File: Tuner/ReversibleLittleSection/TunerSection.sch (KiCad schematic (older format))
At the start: 119 parts, among them J1 Conn_01x03, J10 Conn_01x02, J11 Conn_02x05_Odd_Even, J12 Conn_01x01, J13 Conn_01x01, J14 Conn_01x01, J15 Conn_01x01, J16 Conn_01x01, J17 Conn_01x01, J18 Conn_01x01, J19 Conn_01x01, J2 Conn_01x03, J20 Conn_01x01, J21 Conn_01x01, J22 Conn_01x01, J23 Conn_01x02, J3 Conn_01x03, J4 Conn_01x03, J5 Conn_01x03, J6 Conn_01x03, J7 Conn_01x03, J8 Conn_01x02, J9 Conn_01x02, P10 Conn_01x01, P11 Conn_01x01, P12 Conn_01x01, P2 Conn_01x01, P3 Conn_01x01, P4 Conn_01x01, P5 Conn_01x01, P6 Conn_01x01, P7 Conn_01x01, P8 Conn_01x01, P9 Conn_01x01, U1 MCP23008, U2 ULN2803A

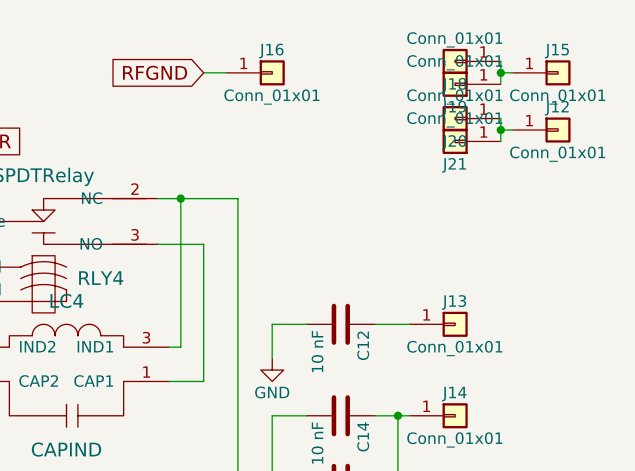
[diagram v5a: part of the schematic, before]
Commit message: Added extra capacitors between relay power and ground posts
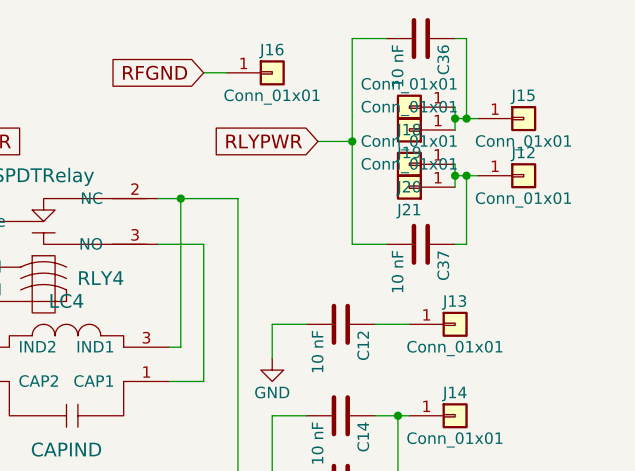
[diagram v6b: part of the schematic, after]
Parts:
- added C36, C37: 10 nF, Capacitors_THT:C_Disc_D5.0mm_W2.5mm_P2.50mm, symbol C
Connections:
- net RLYPWR: now also C36.2, C37.2
- net at J15.1 (Pin_1), J18.1 (Pin_1), J19.1 (Pin_1): now also C36.1
- net at J12.1 (Pin_1), J20.1 (Pin_1), J21.1 (Pin_1): now also C37.1
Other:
- moved on the sheet: J12, J15, J18, J19, J20, J21
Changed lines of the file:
@@
 $EndComp
 $Comp
-L +5V #PWR17
+L +5V #PWR16
 U 1 1 5B1ABFC6
 P 8800 4600
-F 0 "#PWR17" H 8800 4450 50  0001 C CNN
+F 0 "#PWR16" H 8800 4450 50  0001 C CNN
 F 1 "+5V" H 8800 4740 50  0000 C CNN
 F 2 "" H 8800 4600 50  0001 C CNN
@@
 $EndComp
 $Comp
-L GND #PWR18
+L GND #PWR17
 U 1 1 5B1AC04C
 P 8800 5050
-F 0 "#PWR18" H 8800 4800 50  0001 C CNN
+F 0 "#PWR17" H 8800 4800 50  0001 C CNN
 F 1 "GND" H 8800 4900 50  0000 C CNN
 F 2 "" H 8800 5050 50  0001 C CNN
@@
 L Conn_01x01 J15
 U 1 1 5B19812D
-P 11100 750
-F 0 "J15" H 11100 850 50  0000 C CNN
-F 1 "Conn_01x01" H 11100 650 50  0000 C CNN
-F 2 "Connectors:1pin" H 11100 750 50  0001 C CNN
-F 3 "" H 11100 750 50  0001 C CNN
-	1    11100 750
+P 10950 950
+F 0 "J15" H 10950 1050 50  0000 C CNN
+F 1 "Conn_01x01" H 10950 850 50  0000 C CNN
+F 2 "Connectors:1pin" H 10950 950 50  0001 C CNN
+F 3 "" H 10950 950 50  0001 C CNN
+	1    10950 950
 	1    0    0    -1
 $EndComp
@@
 $EndComp
 $Comp
-L GND #PWR19
+L GND #PWR18
 U 1 1 5B982525
 P 9850 2000
-F 0 "#PWR19" H 9850 1750 50  0001 C CNN
+F 0 "#PWR18" H 9850 1750 50  0001 C CNN
 F 1 "GND" H 9850 1850 50  0000 C CNN
 F 2 "" H 9850 2000 50  0001 C CNN
@@
 L Conn_01x01 J18
 U 1 1 5BD8893E
-P 10650 700
-F 0 "J18" H 10650 800 50  0000 C CNN
-F 1 "Conn_01x01" H 10650 600 50  0000 C CNN
-F 2 "tuner:SOLDERJUMPER" H 10650 700 50  0001 C CNN
-F 3 "" H 10650 700 50  0001 C CNN
-	1    10650 700
+P 10450 900
+F 0 "J18" H 10450 1000 50  0000 C CNN
+F 1 "Conn_01x01" H 10450 800 50  0000 C CNN
+F 2 "tuner:SOLDERJUMPER" H 10450 900 50  0001 C CNN
+F 3 "" H 10450 900 50  0001 C CNN
+	1    10450 900
 	-1   0    0    1
 $EndComp
@@
 L Conn_01x01 J19
 U 1 1 5BD88AB6
-P 10650 800
-F 0 "J19" H 10650 900 50  0000 C CNN
-F 1 "Conn_01x01" H 10650 700 50  0000 C CNN
-F 2 "tuner:SOLDERJUMPER" H 10650 800 50  0001 C CNN
-F 3 "" H 10650 800 50  0001 C CNN
-	1    10650 800
+P 10450 1000
+F 0 "J19" H 10450 1100 50  0000 C CNN
+F 1 "Conn_01x01" H 10450 900 50  0000 C CNN
+F 2 "tuner:SOLDERJUMPER" H 10450 1000 50  0001 C CNN
+F 3 "" H 10450 1000 50  0001 C CNN
+	1    10450 1000
 	-1   0    0    1
 $EndComp
@@
 L Conn_01x01 J20
 U 1 1 5BD8922D
-P 10650 950
-F 0 "J20" H 10650 1050 50  0000 C CNN
-F 1 "Conn_01x01" H 10650 850 50  0000 C CNN
-F 2 "tuner:SOLDERJUMPER" H 10650 950 50  0001 C CNN
-F 3 "" H 10650 950 50  0001 C CNN
-	1    10650 950
+P 10450 1150
+F 0 "J20" H 10450 1250 50  0000 C CNN
+F 1 "Conn_01x01" H 10450 1050 50  0000 C CNN
+F 2 "tuner:SOLDERJUMPER" H 10450 1150 50  0001 C CNN
+F 3 "" H 10450 1150 50  0001 C CNN
+	1    10450 1150
 	-1   0    0    1
 $EndComp
@@
 L Conn_01x01 J21
 U 1 1 5BD8939E
-P 10650 1050
-F 0 "J21" H 10650 1150 50  0000 C CNN
-F 1 "Conn_01x01" H 10650 950 50  0000 C CNN
-F 2 "tuner:SOLDERJUMPER" H 10650 1050 50  0001 C CNN
-F 3 "" H 10650 1050 50  0001 C CNN
-	1    10650 1050
+P 10450 1250
+F 0 "J21" H 10450 1350 50  0000 C CNN
+F 1 "Conn_01x01" H 10450 1150 50  0000 C CNN
+F 2 "tuner:SOLDERJUMPER" H 10450 1250 50  0001 C CNN
+F 3 "" H 10450 1250 50  0001 C CNN
+	1    10450 1250
 	-1   0    0    1
 $EndComp
@@
 L Conn_01x01 J12
 U 1 1 5BD8A2D9
-P 11100 1000
-F 0 "J12" H 11100 1100 50  0000 C CNN
-F 1 "Conn_01x01" H 11100 900 50  0000 C CNN
-F 2 "Connectors:1pin" H 11100 1000 50  0001 C CNN
-F 3 "" H 11100 1000 50  0001 C CNN
-	1    11100 1000
-	1    0    0    -1
+P 10950 1200
+F 0 "J12" H 10950 1300 50  0000 C CNN
+F 1 "Conn_01x01" H 10950 1100 50  0000 C CNN
+F 2 "Connectors:1pin" H 10950 1200 50  0001 C CNN
+F 3 "" H 10950 1200 50  0001 C CNN
+	1    10950 1200
+	1    0    0    -1
+$EndComp
+$Comp
+L Conn_01x02 J23
+U 1 1 5C9BB02B
+P 8400 2700
+F 0 "J23" H 8400 2800 50  0000 C CNN
+F 1 "Conn_01x02" H 8400 2500 50  0000 C CNN
+F 2 "tuner:bnc_90_1-1337543-0_pad_combo" H 8400 2700 50  0001 C CNN
+F 3 "" H 8400 2700 50  0001 C CNN
+	1    8400 2700
+	-1   0    0    -1
+$EndComp
+Text GLabel 8950 2800 2    60   Input ~ 0
+RFGND
+Text GLabel 10050 1050 0    60   Input ~ 0
+RLYPWR
+$Comp
+L C C36
+U 1 1 5DDBF507
+P 10500 600
+F 0 "C36" H 10525 700 50  0000 L CNN
+F 1 "10 nF" H 10525 500 50  0000 L CNN
+F 2 "Capacitors_THT:C_Disc_D5.0mm_W2.5mm_P2.50mm" H 10538 450 50  0001 C CNN
+F 3 "" H 10500 600 50  0001 C CNN
+	1    10500 600
+	0    1    1    0
+$EndComp
+$Comp
+L C C37
+U 1 1 5DDBF789
+P 10500 1500
+F 0 "C37" H 10525 1600 50  0000 L CNN
+F 1 "10 nF" H 10525 1400 50  0000 L CNN
+F 2 "Capacitors_THT:C_Disc_D5.0mm_W2.5mm_P2.50mm" H 10538 1350 50  0001 C CNN
+F 3 "" H 10500 1500 50  0001 C CNN
+	1    10500 1500
+	0    1    1    0
 $EndComp
 Connection ~ 10200 5350
@@
 	9650 750  9550 750
 Wire Wire Line
-	10850 700  10850 800
-Wire Wire Line
-	10850 750  10900 750
-Connection ~ 10850 750
-Wire Wire Line
-	10850 950  10850 1050
-Wire Wire Line
-	10850 1000 10900 1000
-Connection ~ 10850 1000
+	10650 900  10650 1000
+Wire Wire Line
+	10650 950  10750 950
+Connection ~ 10650 950
+Wire Wire Line
+	10650 1150 10650 1250
+Wire Wire Line
+	10650 1200 10750 1200
+Connection ~ 10650 1200
 Wire Wire Line
 	10300 4000 10150 4000
@@
 	1850 5200 1850 5300
 Connection ~ 850  5500
-$Comp
-L Conn_01x02 J23
-U 1 1 5C9BB02B
-P 8400 2700
-F 0 "J23" H 8400 2800 50  0000 C CNN
-F 1 "Conn_01x02" H 8400 2500 50  0000 C CNN
-F 2 "tuner:bnc_90_1-1337543-0_pad_combo" H 8400 2700 50  0001 C CNN
-F 3 "" H 8400 2700 50  0001 C CNN
-	1    8400 2700
-	-1   0    0    -1
-$EndComp
 Wire Wire Line
 	8600 2700 8700 2700
@@
 	8500 3100 8500 3200
 Connection ~ 8500 3200
-Text GLabel 8950 2800 2    60   Input ~ 0
-RFGND
 Wire Wire Line
 	8950 2800 8600 2800
+Wire Wire Line
+	10200 1500 10350 1500
+Wire Wire Line
+	10200 600  10200 1500
+Wire Wire Line
+	10200 600  10350 600
+Wire Wire Line
+	10200 1050 10050 1050
+Connection ~ 10200 1050
+Wire Wire Line
+	10700 950  10700 600
+Wire Wire Line
+	10700 600  10650 600
+Connection ~ 10700 950
+Wire Wire Line
+	10700 1200 10700 1500
+Wire Wire Line
+	10700 1500 10650 1500
+Connection ~ 10700 1200
 $EndSCHEMATC

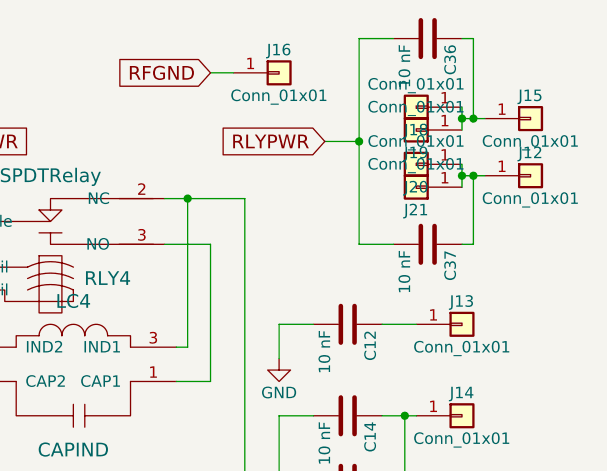
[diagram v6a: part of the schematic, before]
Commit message: Changed some of the capacitors to NC becaue they might cause problems in some situations
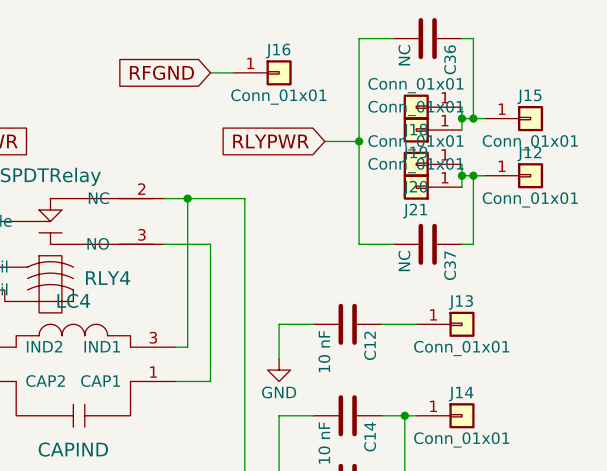
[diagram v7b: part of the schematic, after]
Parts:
- C36, C37: value 10 nF -> NC
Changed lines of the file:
@@
 P 10500 600
 F 0 "C36" H 10525 700 50  0000 L CNN
-F 1 "10 nF" H 10525 500 50  0000 L CNN
+F 1 "NC" H 10525 500 50  0000 L CNN
 F 2 "Capacitors_THT:C_Disc_D5.0mm_W2.5mm_P2.50mm" H 10538 450 50  0001 C CNN
 F 3 "" H 10500 600 50  0001 C CNN
@@
 P 10500 1500
 F 0 "C37" H 10525 1600 50  0000 L CNN
-F 1 "10 nF" H 10525 1400 50  0000 L CNN
+F 1 "NC" H 10525 1400 50  0000 L CNN
 F 2 "Capacitors_THT:C_Disc_D5.0mm_W2.5mm_P2.50mm" H 10538 1350 50  0001 C CNN
 F 3 "" H 10500 1500 50  0001 C CNN

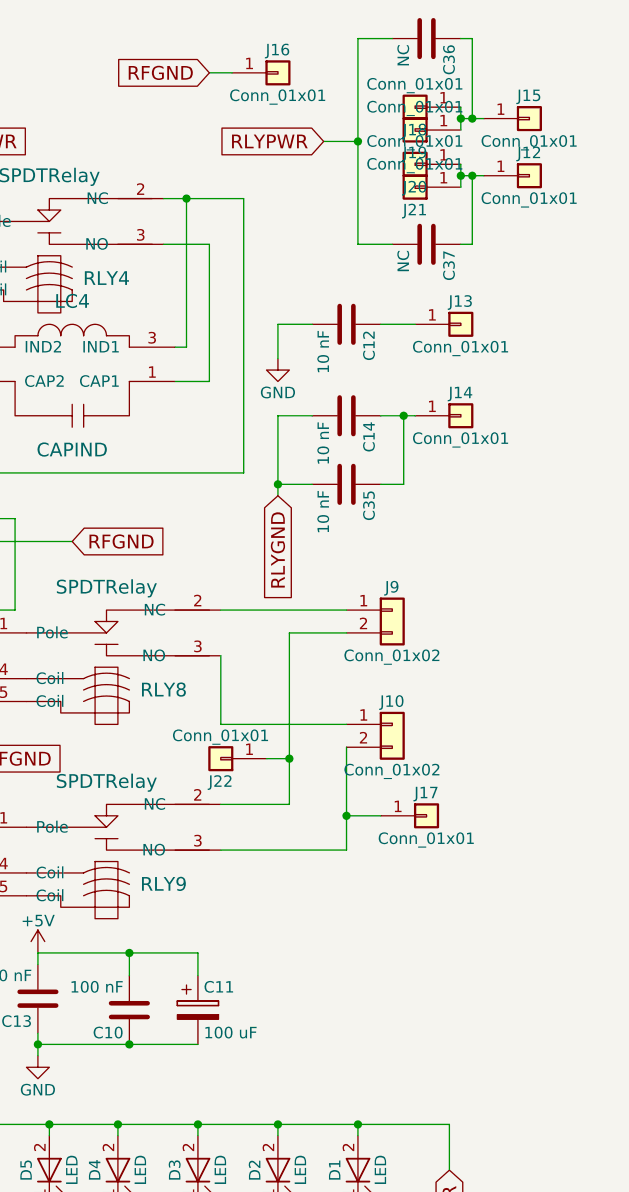
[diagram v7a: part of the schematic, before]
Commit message: Added extra mounting holes to ground ReversibleLittleSection
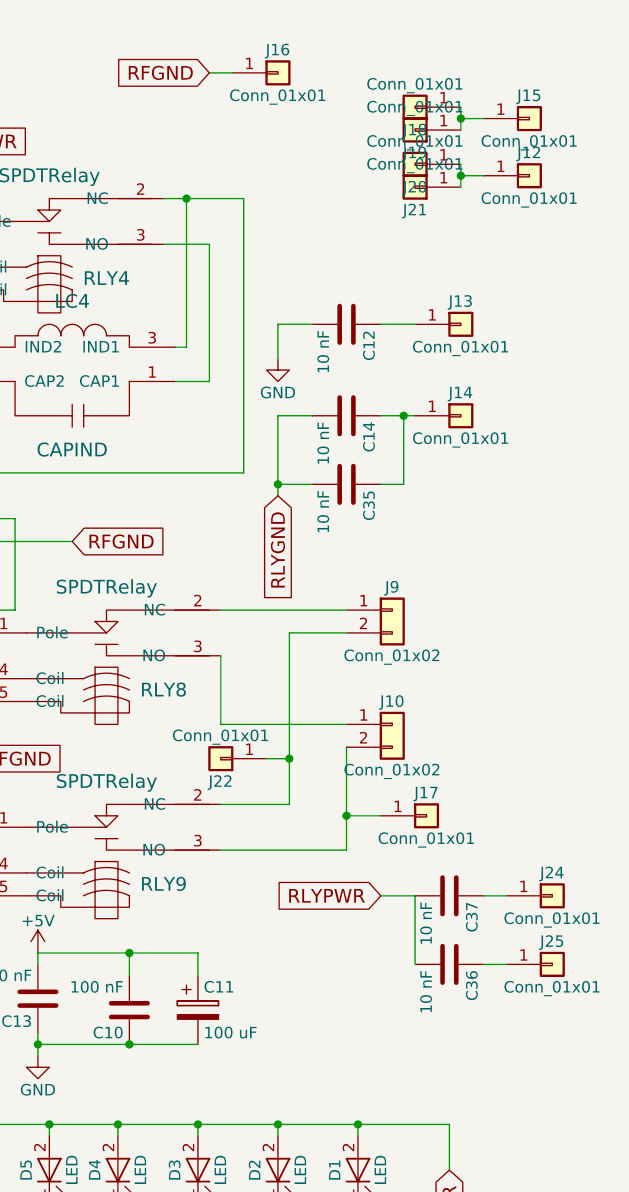
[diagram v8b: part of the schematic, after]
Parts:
- added J24, J25: Conn_01x01, Connectors:1pin, symbol Conn_01x01
- C36, C37: value NC -> 10 nF
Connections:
- net at J15.1 (Pin_1), J18.1 (Pin_1), J19.1 (Pin_1): no longer C36.1
- net at J12.1 (Pin_1), J20.1 (Pin_1), J21.1 (Pin_1): no longer C37.1
- new net: C36.1, J25.1 (Pin_1)
- new net: C37.1, J24.1 (Pin_1)
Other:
- moved on the sheet: C36, C37
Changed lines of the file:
@@
 RLY8
 $Comp
-L +5V #PWR12
+L +5V #PWR01
 U 1 1 5B1A0287
 P 3150 5750
-F 0 "#PWR12" H 3150 5600 50  0001 C CNN
+F 0 "#PWR01" H 3150 5600 50  0001 C CNN
 F 1 "+5V" H 3150 5890 50  0000 C CNN
 F 2 "" H 3150 5750 50  0001 C CNN
@@
 $EndComp
 $Comp
-L GND #PWR3
+L GND #PWR02
 U 1 1 5B1AA0F6
 P 900 4500
-F 0 "#PWR3" H 900 4250 50  0001 C CNN
+F 0 "#PWR02" H 900 4250 50  0001 C CNN
 F 1 "GND" H 900 4350 50  0000 C CNN
 F 2 "" H 900 4500 50  0001 C CNN
@@
 $EndComp
 $Comp
-L +5V #PWR2
+L +5V #PWR03
 U 1 1 5B1AABE9
 P 900 3750
-F 0 "#PWR2" H 900 3600 50  0001 C CNN
+F 0 "#PWR03" H 900 3600 50  0001 C CNN
 F 1 "+5V" H 900 3890 50  0000 C CNN
 F 2 "" H 900 3750 50  0001 C CNN
@@
 $EndComp
 $Comp
-L +5V #PWR8
+L +5V #PWR04
 U 1 1 5B1ABA5A
 P 2150 4450
-F 0 "#PWR8" H 2150 4300 50  0001 C CNN
+F 0 "#PWR04" H 2150 4300 50  0001 C CNN
 F 1 "+5V" H 2150 4590 50  0000 C CNN
 F 2 "" H 2150 4450 50  0001 C CNN
@@
 $EndComp
 $Comp
-L +5V #PWR10
+L +5V #PWR05
 U 1 1 5B1ABCDE
 P 2400 3950
-F 0 "#PWR10" H 2400 3800 50  0001 C CNN
+F 0 "#PWR05" H 2400 3800 50  0001 C CNN
 F 1 "+5V" H 2400 4090 50  0000 C CNN
 F 2 "" H 2400 3950 50  0001 C CNN
@@
 $EndComp
 $Comp
-L +5V #PWR16
+L +5V #PWR06
 U 1 1 5B1ABFC6
 P 8800 4600
-F 0 "#PWR16" H 8800 4450 50  0001 C CNN
+F 0 "#PWR06" H 8800 4450 50  0001 C CNN
 F 1 "+5V" H 8800 4740 50  0000 C CNN
 F 2 "" H 8800 4600 50  0001 C CNN
@@
 $EndComp
 $Comp
-L GND #PWR17
+L GND #PWR07
 U 1 1 5B1AC04C
 P 8800 5050
-F 0 "#PWR17" H 8800 4800 50  0001 C CNN
+F 0 "#PWR07" H 8800 4800 50  0001 C CNN
 F 1 "GND" H 8800 4900 50  0000 C CNN
 F 2 "" H 8800 5050 50  0001 C CNN
@@
 $EndComp
 $Comp
-L +5V #PWR9
+L +5V #PWR08
 U 1 1 5B196BCE
 P 2250 3950
-F 0 "#PWR9" H 2250 3800 50  0001 C CNN
+F 0 "#PWR08" H 2250 3800 50  0001 C CNN
 F 1 "+5V" H 2250 4090 50  0000 C CNN
 F 2 "" H 2250 3950 50  0001 C CNN
@@
 $EndComp
 $Comp
-L GND #PWR14
+L GND #PWR09
 U 1 1 5B9A4AE1
 P 4850 6650
-F 0 "#PWR14" H 4850 6400 50  0001 C CNN
+F 0 "#PWR09" H 4850 6400 50  0001 C CNN
 F 1 "GND" H 4850 6500 50  0000 C CNN
 F 2 "" H 4850 6650 50  0001 C CNN
@@
 $EndComp
 $Comp
-L GND #PWR11
+L GND #PWR010
 U 1 1 5B9A6036
 P 3150 4200
-F 0 "#PWR11" H 3150 3950 50  0001 C CNN
+F 0 "#PWR010" H 3150 3950 50  0001 C CNN
 F 1 "GND" H 3150 4050 50  0000 C CNN
 F 2 "" H 3150 4200 50  0001 C CNN
@@
 $EndComp
 $Comp
-L GND #PWR13
+L GND #PWR011
 U 1 1 5B9ACA36
 P 3550 6100
-F 0 "#PWR13" H 3550 5850 50  0001 C CNN
+F 0 "#PWR011" H 3550 5850 50  0001 C CNN
 F 1 "GND" H 3550 5950 50  0000 C CNN
 F 2 "" H 3550 6100 50  0001 C CNN
@@
 $EndComp
 $Comp
-L GND #PWR18
+L GND #PWR012
 U 1 1 5B982525
 P 9850 2000
-F 0 "#PWR18" H 9850 1750 50  0001 C CNN
+F 0 "#PWR012" H 9850 1750 50  0001 C CNN
 F 1 "GND" H 9850 1850 50  0000 C CNN
 F 2 "" H 9850 2000 50  0001 C CNN
@@
 $EndComp
 $Comp
-L GND #PWR7
+L GND #PWR013
 U 1 1 5BA4D8F3
 P 1800 5850
-F 0 "#PWR7" H 1800 5600 50  0001 C CNN
+F 0 "#PWR013" H 1800 5600 50  0001 C CNN
 F 1 "GND" H 1800 5700 50  0000 C CNN
 F 2 "" H 1800 5850 50  0001 C CNN
@@
 $EndComp
 $Comp
-L +5V #PWR6
+L +5V #PWR014
 U 1 1 5BA4E663
 P 1200 5700
-F 0 "#PWR6" H 1200 5550 50  0001 C CNN
+F 0 "#PWR014" H 1200 5550 50  0001 C CNN
 F 1 "+5V" H 1200 5840 50  0000 C CNN
 F 2 "" H 1200 5700 50  0001 C CNN
@@
 $EndComp
 $Comp
-L GND #PWR1
+L GND #PWR015
 U 1 1 5BA4FB25
 P 750 5900
-F 0 "#PWR1" H 750 5650 50  0001 C CNN
+F 0 "#PWR015" H 750 5650 50  0001 C CNN
 F 1 "GND" H 750 5750 50  0000 C CNN
 F 2 "" H 750 5900 50  0001 C CNN
@@
 $EndComp
 $Comp
-L GND #PWR5
+L GND #PWR016
 U 1 1 5BA5005D
 P 1100 5300
-F 0 "#PWR5" H 1100 5050 50  0001 C CNN
+F 0 "#PWR016" H 1100 5050 50  0001 C CNN
 F 1 "GND" H 1100 5150 50  0000 C CNN
 F 2 "" H 1100 5300 50  0001 C CNN
@@
 EXTPWR
 $Comp
-L +5V #PWR4
+L +5V #PWR017
 U 1 1 5BAE4DBC
 P 1000 4850
-F 0 "#PWR4" H 1000 4700 50  0001 C CNN
+F 0 "#PWR017" H 1000 4700 50  0001 C CNN
 F 1 "+5V" H 1000 4990 50  0000 C CNN
 F 2 "" H 1000 4850 50  0001 C CNN
@@
 $EndComp
 $Comp
-L GND #PWR15
+L GND #PWR018
 U 1 1 5BAEE216
 P 5050 7250
-F 0 "#PWR15" H 5050 7000 50  0001 C CNN
+F 0 "#PWR018" H 5050 7000 50  0001 C CNN
 F 1 "GND" H 5050 7100 50  0000 C CNN
 F 2 "" H 5050 7250 50  0001 C CNN
@@
 Text GLabel 8950 2800 2    60   Input ~ 0
 RFGND
-Text GLabel 10050 1050 0    60   Input ~ 0
+Text GLabel 10300 4350 0    60   Input ~ 0
 RLYPWR
 $Comp
 L C C36
 U 1 1 5DDBF507
-P 10500 600
-F 0 "C36" H 10525 700 50  0000 L CNN
-F 1 "NC" H 10525 500 50  0000 L CNN
-F 2 "Capacitors_THT:C_Disc_D5.0mm_W2.5mm_P2.50mm" H 10538 450 50  0001 C CNN
-F 3 "" H 10500 600 50  0001 C CNN
-	1    10500 600
+P 10600 4650
+F 0 "C36" H 10625 4750 50  0000 L CNN
+F 1 "10 nF" H 10625 4550 50  0000 L CNN
+F 2 "Capacitors_THT:C_Disc_D5.0mm_W2.5mm_P2.50mm" H 10638 4500 50  0001 C CNN
+F 3 "" H 10600 4650 50  0001 C CNN
+	1    10600 4650
 	0    1    1    0
 $EndComp
@@
 L C C37
 U 1 1 5DDBF789
-P 10500 1500
-F 0 "C37" H 10525 1600 50  0000 L CNN
-F 1 "NC" H 10525 1400 50  0000 L CNN
-F 2 "Capacitors_THT:C_Disc_D5.0mm_W2.5mm_P2.50mm" H 10538 1350 50  0001 C CNN
-F 3 "" H 10500 1500 50  0001 C CNN
-	1    10500 1500
+P 10600 4350
+F 0 "C37" H 10625 4450 50  0000 L CNN
+F 1 "10 nF" H 10625 4250 50  0000 L CNN
+F 2 "Capacitors_THT:C_Disc_D5.0mm_W2.5mm_P2.50mm" H 10638 4200 50  0001 C CNN
+F 3 "" H 10600 4350 50  0001 C CNN
+	1    10600 4350
 	0    1    1    0
 $EndComp
@@
 	8950 2800 8600 2800
 Wire Wire Line
-	10200 1500 10350 1500
-Wire Wire Line
-	10200 600  10200 1500
-Wire Wire Line
-	10200 600  10350 600
-Wire Wire Line
-	10200 1050 10050 1050
-Connection ~ 10200 1050
-Wire Wire Line
-	10700 950  10700 600
-Wire Wire Line
-	10700 600  10650 600
-Connection ~ 10700 950
-Wire Wire Line
-	10700 1200 10700 1500
-Wire Wire Line
-	10700 1500 10650 1500
-Connection ~ 10700 1200
+	10450 4650 10450 4350
+Wire Wire Line
+	10450 4350 10300 4350
+$Comp
+L Conn_01x01 J24
+U 1 1 5DE1B51D
+P 11050 4350
+F 0 "J24" H 11050 4450 50  0000 C CNN
+F 1 "Conn_01x01" H 11050 4250 50  0000 C CNN
+F 2 "Connectors:1pin" H 11050 4350 50  0001 C CNN
+F 3 "" H 11050 4350 50  0001 C CNN
+	1    11050 4350
+	1    0    0    -1
+$EndComp
+$Comp
+L Conn_01x01 J25
+U 1 1 5DE1B7B9
+P 11050 4650
+F 0 "J25" H 11050 4750 50  0000 C CNN
+F 1 "Conn_01x01" H 11050 4550 50  0000 C CNN
+F 2 "Connectors:1pin" H 11050 4650 50  0001 C CNN
+F 3 "" H 11050 4650 50  0001 C CNN
+	1    11050 4650
+	1    0    0    -1
+$EndComp
+Wire Wire Line
+	10750 4650 10850 4650
+Wire Wire Line
+	10850 4350 10750 4350
 $EndSCHEMATC
